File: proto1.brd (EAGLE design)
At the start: 100 x 80 mm, 10 parts, among them U1 RASPBERRY_PICOTH, U2 GY-521MPU6050, U3 HMC5883LGY-271, U4 ESP8266_ESP-01

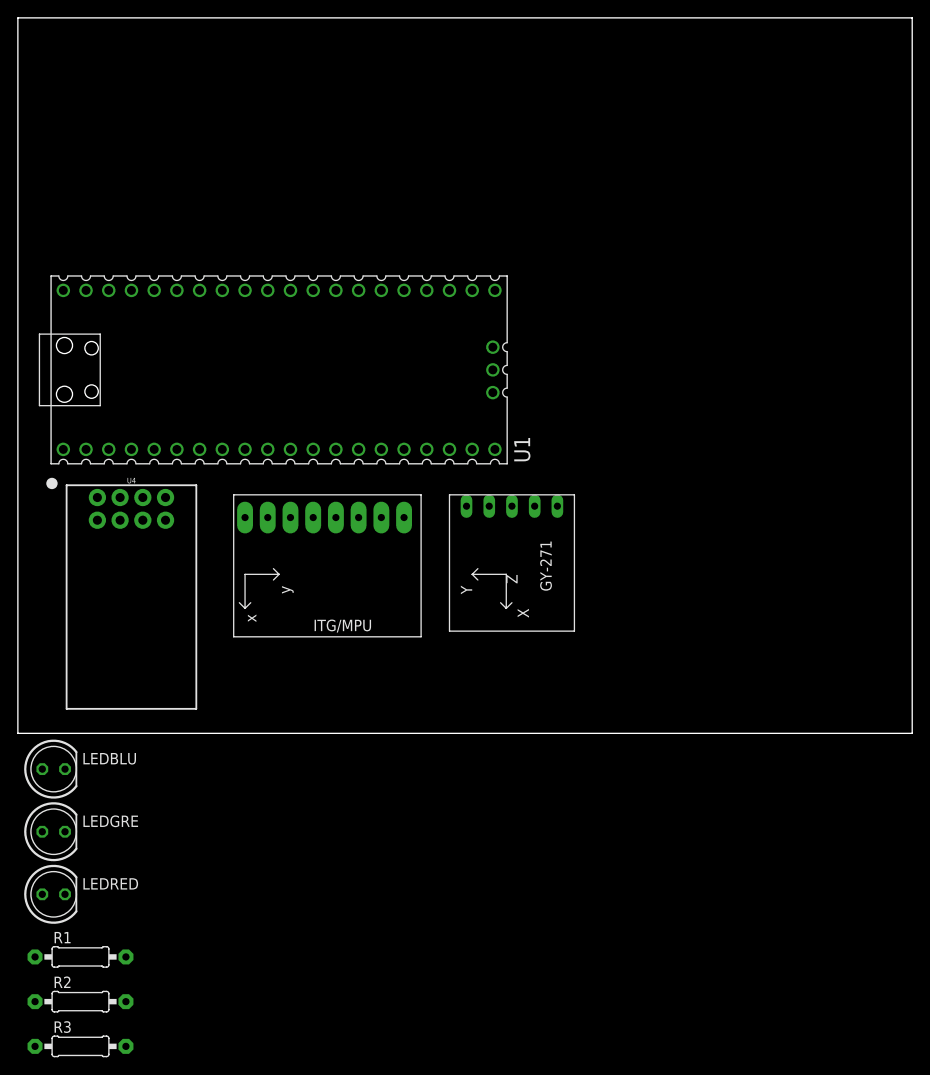
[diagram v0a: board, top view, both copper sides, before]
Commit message: Change microcontroller
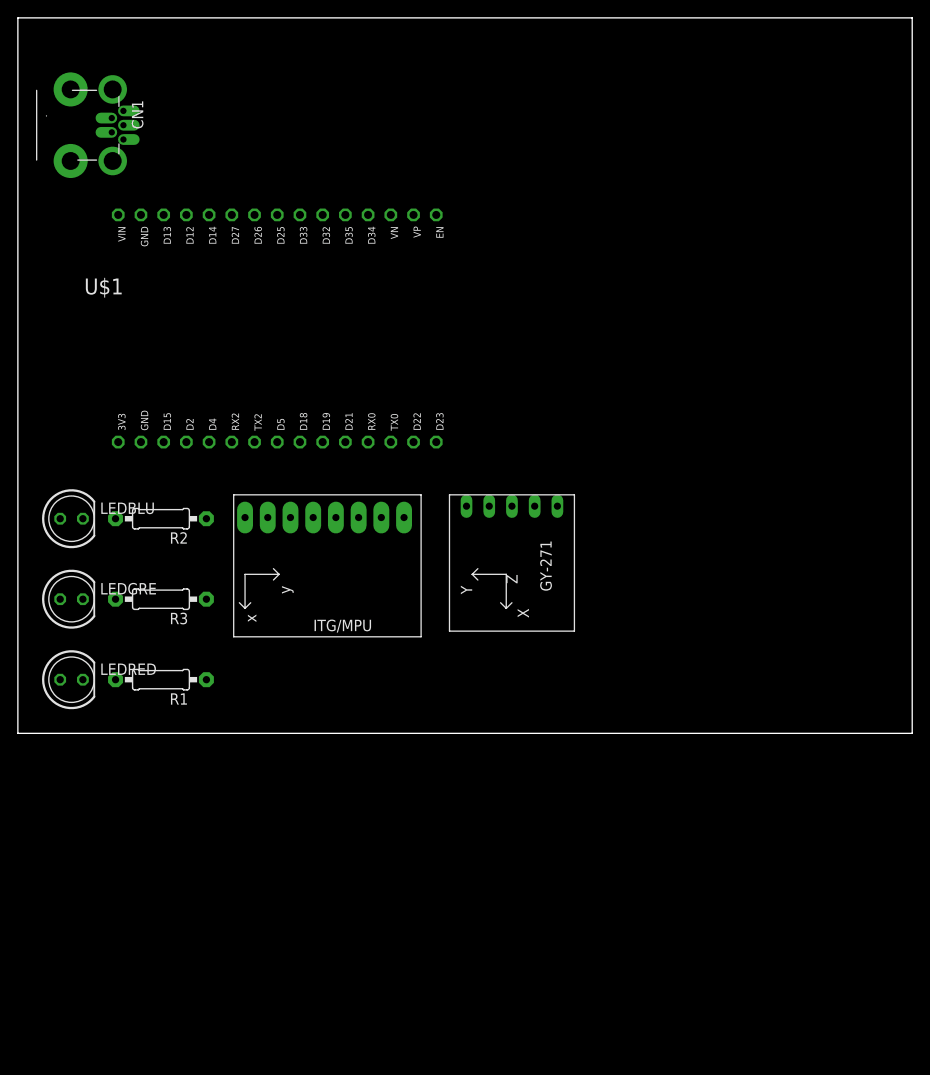
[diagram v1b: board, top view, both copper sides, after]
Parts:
- removed U1: RASPBERRY_PICOTH, RpiPico:PICO-PKG-TH
- removed U4: ESP8266_ESP-01, SparkFun-RF:ESP8266_ESP-01
- added CN1: (no value), adafruit:USB-MINIB-THM
- added U$1: ESP32_DEVKIT, DOIT_ESP32_DEVKIT:ESP32_DEVKIT
- moved R2 54.7 mm to (16.0, 24.0), turned to 180 degrees
- moved R3 50.8 mm to (16.0, 15.0), turned to 180 degrees
- moved R1 32.3 mm to (16.0, 6.00), turned to 180 degrees
- moved LEDBLU 28.1 mm to (6.00, 24.0)
- moved LEDGRE 26.1 mm to (6.00, 15.0)
- moved LEDRED 24.1 mm to (6.00, 6.00)
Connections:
- removed net N$10: U3.SCL
- removed net N$11: U3.SDA
- removed net N$2: U4.3
- removed net N$5: U2.XDA
- removed net N$6: U2.XCL
- removed net N$7: U4.7
- removed net RX: U1.2, U4.5
- removed net SWGND: U1.42
- removed net TX: U1.1, U4.1
- removed net VBUS: U1.40
- removed net VSYS: U1.39
- new net XCL: U2.XCL, U3.SCL
- new net XDA: U2.XDA, U3.SDA
- net GND: now also CN1.GND, U$1.GND@1, U$1.GND@2; no longer U1.13, U1.18, U1.23, U1.28, U1.3, U1.33, U1.38, U1.8, U4.6, U4.8
- net LEDBLU: now also U$1.D35; no longer U1.16
- net LEDGRE: now also U$1.D32; no longer U1.14
- net LEDRED: now also U$1.D34; no longer U1.15
- net SCL: now also U$1.D22; no longer U1.7
- net SDA: now also U$1.D21; no longer U1.6
- net VCC: now also CN1.VBUS, U$1.3V3; no longer U1.36, U4.2, U4.4
